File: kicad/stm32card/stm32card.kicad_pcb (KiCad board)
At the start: 2 copper layers, 48 parts, among them SW1 TSD003A04126A02, SW2 TSD003A04126A02, SW3 TSD003A04126A02, SW4 TSD003A04126A02, SW5 TSD003A04126A02, SW6 TSD003A04126A02, SW8 TSD003A04126A02, U2 MT9216, U3 N096-1608TBBIG11-H13, U4 STM32F103C8T6

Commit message: rev1a
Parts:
- removed BAT1, BAT2, BAT3, BAT4: 2997, indigos_kicad_lib:2997_KEY
- removed C20: 10uF, Capacitor_SMD:C_0603_1608Metric
- removed C21: 100nF, Capacitor_SMD:C_0603_1608Metric
- removed the C3 at (91.2, 105.5)
- removed the C6 at (91.2, 113.1)
- removed the R3 at (99.2, 110.5)
- removed SW8: TSD003A04126A02, easyeda2kicad:SW-SMD_4P-L6.0-W6.0-P4.50-LS8.6
- added G***: LOGO, LOGO, F.Cu at (139.8, 122.7)
- added G***: LOGO, LOGO, F.Cu at (139.8, 112.1)
- added G***: LOGO, LOGO, B.Cu at (154.5, 103.7)
- added J1: USB_C_Receptacle_PowerOnly_6P, indigos_kicad_lib:SAMESKY_UJC-H-G-SMT-2-P6-TR, F.Cu at (142.1, 84.3)
- added R1: 5.1k, Resistor_SMD:R_0603_1608Metric, F.Cu at (141.3, 90.8)
- added R2: 5.1k, Resistor_SMD:R_0603_1608Metric, F.Cu at (142.8, 90.8)
- added SWCLK1: SWCLK, TestPoint:TestPoint_Pad_D2.0mm, F.Cu at (165.3, 129.6)
- added SWDIO1: SWDIO, TestPoint:TestPoint_Pad_D2.0mm, F.Cu at (164.8, 124.3)
- added TP1: 675_positive, TestPoint:TestPoint_Pad_4.0x4.0mm, F.Cu at (151.3, 90.0)
- added TP_mosi1: TestPoint, TestPoint:TestPoint_Pad_D2.0mm, F.Cu at (174.4, 114.2)
- added TP_sck1: TestPoint, TestPoint:TestPoint_Pad_D2.0mm, F.Cu at (178.4, 108.9)
- added TestPoint_gnd1: TestPoint_gnd, TestPoint:TestPoint_Pad_D2.0mm, F.Cu at (155.7, 99.1)
- added U2: LM66100DCK, Package_TO_SOT_SMD:SOT-363_SC-70-6, F.Cu at (145.0, 96.6)
- added U3: LM66100DCK, Package_TO_SOT_SMD:SOT-363_SC-70-6, F.Cu at (148.4, 96.6)
- added U6: ~, Library:battery_holder, F.Cu at (167.8, 90.0)
- added tst_nrst1: tst_nrst, TestPoint:TestPoint_Pad_D2.0mm, F.Cu at (180.0, 127.3)
- added unreg_vcc1: unreg_vcc, TestPoint:TestPoint_Pad_D2.0mm, F.Cu at (159.0, 99.1)
- C1: value 4.7uF -> 10uF
- C8: value 10uF -> 2.2uF
- L1: footprint Inductor_SMD:L_0603_1608Metric -> indigos_kicad_lib:IND-SMD_L5.8-W5.2
- R3: renamed from R1; footprint Resistor_SMD:R_0603_1608Metric -> Resistor_SMD:R_0805_2012Metric
- R4: renamed from R2; value 100k 1% -> 100k .01%; footprint Resistor_SMD:R_0603_1608Metric -> Resistor_SMD:R_0805_2012Metric
- moved b_left1 132.0 mm to (215.0, 115.4)
- moved b_down1 131.3 mm to (207.0, 123.8), turned to 180 degrees
- moved b_up1 128.3 mm to (207.0, 106.9)
- moved b_right1 119.0 mm to (199.0, 115.4)
- moved C14 92.9 mm to (187.4, 122.4)
- moved C16 92.4 mm to (187.3, 120.5)
- moved C15 92.0 mm to (187.3, 118.0)
- moved C8 87.8 mm to (179.0, 121.7), turned to 180 degrees
- moved C5 87.8 mm to (179.0, 123.1)
- moved C13 87.7 mm to (182.5, 116.4)
- moved R6 85.4 mm to (184.4, 122.4)
- moved R9 85.1 mm to (184.3, 120.5)
- moved C12 84.2 mm to (176.7, 126.8)
- moved C6 83.7 mm to (174.9, 128.5)
- moved C11 83.3 mm to (179.0, 124.6)
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- renumbered C19 to C11, C17 to C15, C15 to C16, C16 to C17, C5 to C2, C4 to C3, C7 to C4, C9 to C5, C11 to C6, C2 to C9, R11 to R10, R12 to R11, R7 to R12, R9 to R13, R4 to R5, R5 to R6, R8 to R7, R10 to R8, R6 to R9, U2 to U1, U3 to U5, SW4 to b_a1, SW6 to b_b1, SW2 to b_down1, SW5 to b_left1, SW3 to b_right1, SW1 to b_up1
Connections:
- net Net-(U2-EN) renamed unregulated_vcc
- net reset_button renamed Net-(U4-NRST)
- C13 pad 2: Net-(C13-Pad2) -> in_button_up
- C14 pad 2: Net-(C14-Pad2) -> in_button_down
- C15 pad 2: Net-(C17-Pad2) -> in_button_left
- C16 pad 2: Net-(C15-Pad2) -> in_button_right
- C17 pad 2: Net-(C16-Pad2) -> in_button_a
- C18 pad 2: Net-(C18-Pad2) -> in_button_b
- C8 pad 1: +3V0 -> GND
- C8 pad 2: GND -> +3V0
- U4 pad 10: unconnected-(U4-PA0-WKUP-Pad10) -> in_button_down
- U4 pad 11: unconnected-(U4-PA1-Pad11) -> in_button_right
- U4 pad 12: unconnected-(U4-PA2-Pad12) -> in_button_left
- U4 pad 13: unconnected-(U4-PA3-Pad13) -> in_button_up
- U4 pad 18: button_up -> lcd_dataselect
- U4 pad 19: button_down -> lcd_reset
- U4 pad 20: button_left -> lcd_cs
- U4 pad 25: unconnected-(U4-PB12-Pad25) -> power_info
- U4 pad 26: unconnected-(U4-PB13-Pad26) -> in_button_a
- U4 pad 27: unconnected-(U4-PB14-Pad27) -> in_button_b
- U4 pad 34: unconnected-(U4-PA13-Pad34) -> Net-(U4-PA13)
- U4 pad 37: unconnected-(U4-PA14-Pad37) -> Net-(U4-PA14)
- U4 pad 39: button_right -> unconnected-(U4-PB3-Pad39)
- U4 pad 40: button_a -> unconnected-(U4-PB4-Pad40)
- U4 pad 41: button_b -> unconnected-(U4-PB5-Pad41)
- U4 pad 42: Net-(U3-CS) -> unconnected-(U4-PB6-Pad42)
- U4 pad 43: Net-(U3-RESET) -> unconnected-(U4-PB7-Pad43)
- U4 pad 45: Net-(U3-RS) -> unconnected-(U4-PB8-Pad45)
- U5 pad 5: Net-(U3-RS) -> lcd_dataselect
- U5 pad 6: Net-(U3-RESET) -> lcd_reset
- U5 pad 7: Net-(U3-CS) -> lcd_cs
- b_a1 pad 3: button_a -> in_button_a
- b_a1 pad 4: Net-(C16-Pad2) -> in_button_a
- b_b1 pad 3: button_b -> in_button_b
- b_b1 pad 4: Net-(C18-Pad2) -> in_button_b
- b_down1 pad 3: button_down -> in_button_down
- b_down1 pad 4: Net-(C14-Pad2) -> in_button_down
- b_left1 pad 3: button_left -> in_button_left
- b_left1 pad 4: Net-(C17-Pad2) -> in_button_left
- b_right1 pad 3: button_right -> in_button_right
- b_right1 pad 4: Net-(C15-Pad2) -> in_button_right
- b_up1 pad 3: button_up -> in_button_up
- b_up1 pad 4: Net-(C13-Pad2) -> in_button_up
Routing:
- net +3V0: track 0.00 -> 257.7 mm
- net GND: track 0.00 -> 190.9 mm, vias 0 -> 34
- net in_button_left: track 0.00 -> 44.4 mm
- net in_button_up: track 0.00 -> 40.0 mm
- net power_info: track 0.00 -> 39.5 mm
- net in_button_down: track 0.00 -> 35.8 mm
- net in_button_a: track 0.00 -> 30.9 mm
- net in_button_right: track 0.00 -> 28.8 mm
- net in_button_b: track 0.00 -> 27.8 mm
- net unregulated_vcc: track 0.00 -> 23.0 mm
- net Net-(U2-~{CE}): track 0.00 -> 18.7 mm
- net spi1_sck: track 0.00 -> 15.6 mm
- net spi1_mosi: track 0.00 -> 14.9 mm
- net lcd_cs: track 0.00 -> 13.6 mm
- net lcd_reset: track 0.00 -> 12.6 mm
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- added copper zone on B.Cu, net GND
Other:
- board outline added: 88.9 x 50.8 mm
- board text added: "(913) 228-6776"
- board text added: "Brett Weiland"
- board text added: "Electrical and Computer Engineer"
- board text added: "bpcspace.com"
- board text added: "brettsweiland@gmail.com"
- board text added: "mandrelcard.alpha.01"
- board text removed: "CHECK PAGAGES!!!!! 10/40k resistor, inductor are wrong!!!"

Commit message: applying 4 more jobs
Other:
- board text added: "BEFORE RE-ORDERING: - fix routing to MCU; footprint was changed - fix vtext - SPI NSI - LEDs? - change your god damn test pins - remove if no more needed - remove button outlines - SPI speed stuck at 2mHZ - differential routing? - LCD backlight MOSFTER - test to see if sleep mode is accurate to datasheet - screen responds in sleep mode, which is sus - add mosfet to LED VDD if above is too sus"

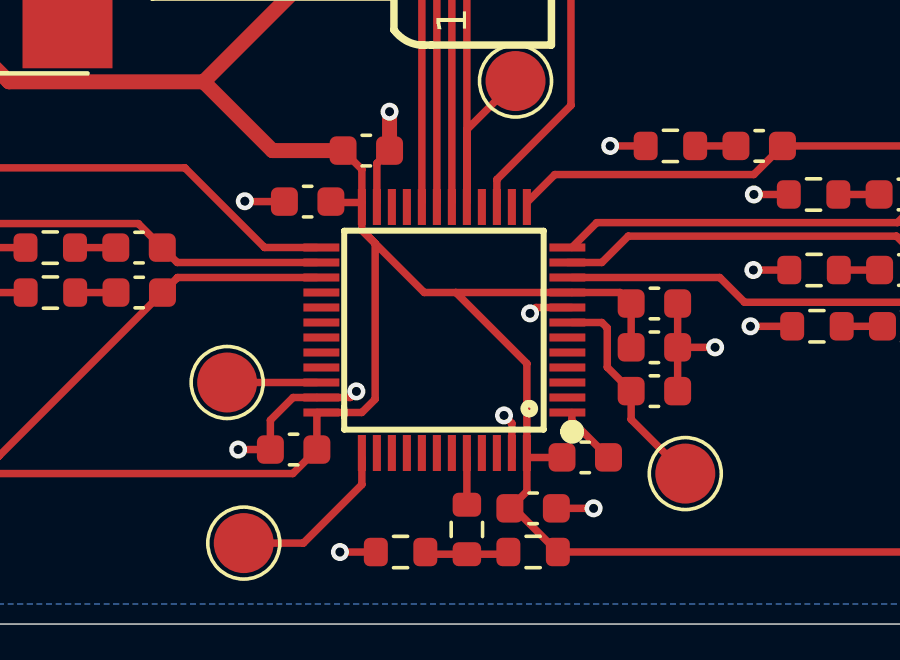
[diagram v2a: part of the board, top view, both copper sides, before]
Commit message: optimized spi
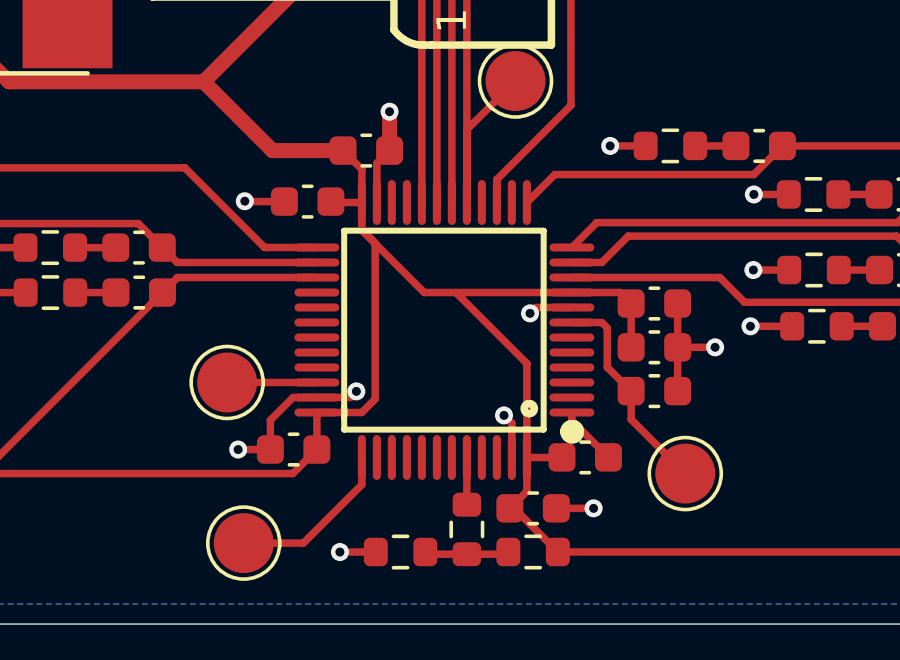
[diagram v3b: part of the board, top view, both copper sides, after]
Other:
- board text removed: "BEFORE RE-ORDERING: - fix routing to MCU; footprint was changed - fix vtext - SPI NSI - LEDs? - change your god damn test pins - remove if no more needed - remove button outlines - SPI speed stuck at 2mHZ - differential routing? - LCD backlight MOSFTER - test to see if sleep mode is accurate to datasheet - screen responds in sleep mode, which is sus - add mosfet to LED VDD if above is too sus"

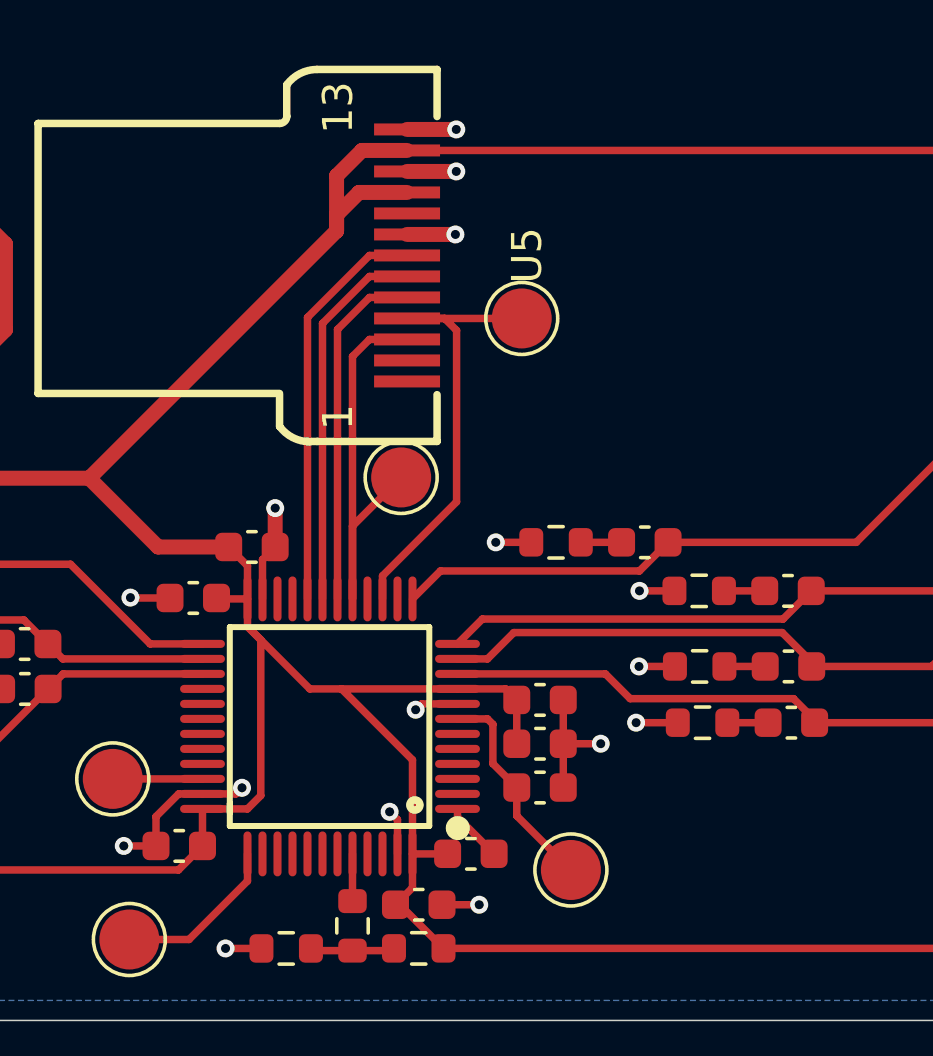
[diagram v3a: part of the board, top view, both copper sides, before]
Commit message: optimized spi
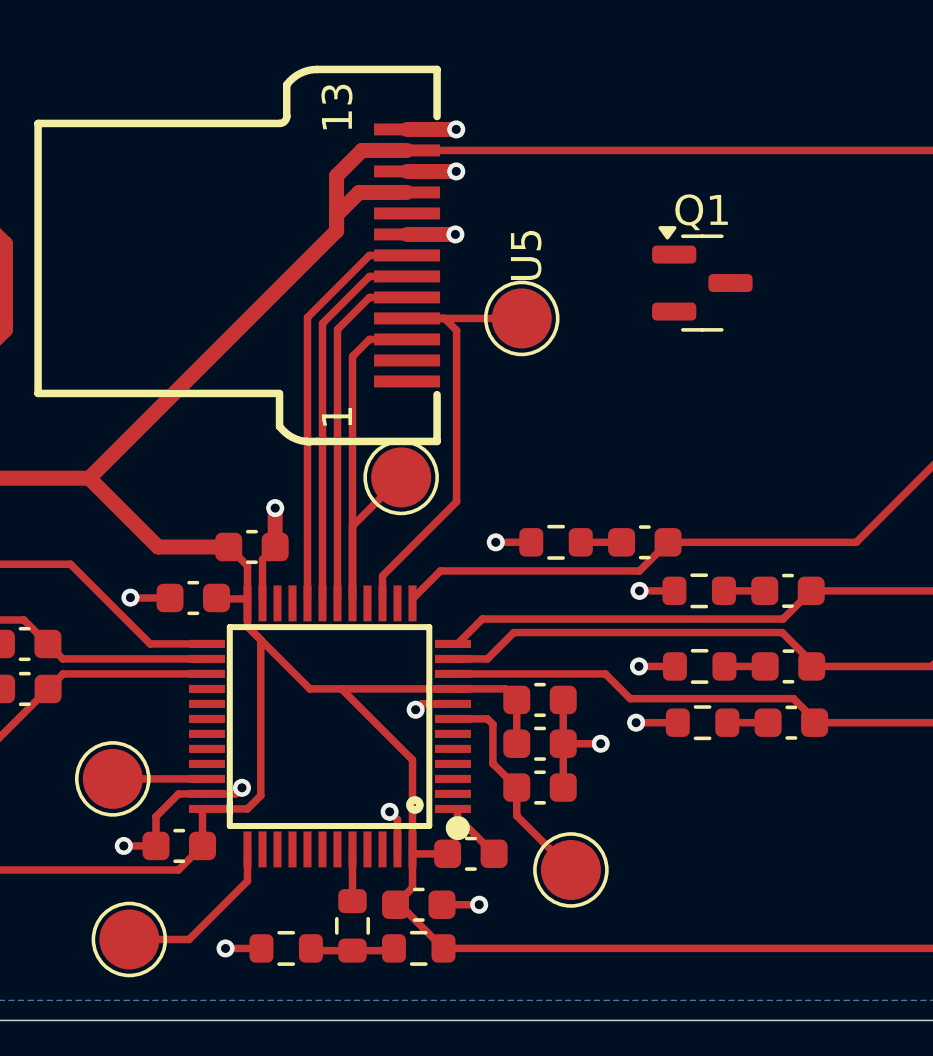
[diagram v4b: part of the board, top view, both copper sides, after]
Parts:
- added Q1: AO3400A, Package_TO_SOT_SMD:SOT-23, F.Cu at (184.4, 107.8)
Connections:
- U4 pad 21: unconnected-(U4-PB10-Pad21) -> backlight_fet
- U5 pad 12: +3V0 -> Net-(Q1-S)
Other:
- board text added: "BEFORE RE-ORDERING: - fix routing to MCU; footprint was changed - fix vtext - SPI NSI - LEDs? - change your god damn test pins - remove if no more needed - remove button outlines - SPI speed stuck at 2mHZ - differential routing? - LCD backlight MOSFTER - test to see if sleep mode is accurate to datasheet - screen responds in sleep mode, which is sus - add mosfet to LED VDD if above is too sus"

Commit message: about to add border tracing, thick in the weeds
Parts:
- removed the G*** at (139.8, 112.1)
- moved Q1 26.3 mm to (159.3, 115.5), turned to 180 degrees
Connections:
- U4 pad 21: backlight_fet -> unconnected-(U4-PB10-Pad21)
- U4 pad 28: unconnected-(U4-PB15-Pad28) -> backlight_fet
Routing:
- net Net-(Q1-S): track 0.00 -> 18.4 mm
- net backlight_fet: track 0.00 -> 12.9 mm
- net +3V0: track 257.7 -> 253.7 mm

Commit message: need to organize, redid PCB
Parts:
- removed R3: 400k 1%, Resistor_SMD:R_0805_2012Metric
- removed unreg_vcc1: unreg_vcc, TestPoint:TestPoint_Pad_D2.0mm
- added BT1: NiMH AAA cell, Battery:BatteryHolder_Keystone_2466_1xAAA, F.Cu at (171.7, 90.8)
- added C19: 1nF, Capacitor_SMD:C_0603_1608Metric, F.Cu at (154.8, 111.9)
- added C20: 1uF, Capacitor_SMD:C_0603_1608Metric, F.Cu at (155.5, 117.2)
- added C21: 1uF, Capacitor_SMD:C_0603_1608Metric, F.Cu at (153.6, 119.1)
- added C22: 10uF, Capacitor_SMD:C_0603_1608Metric, F.Cu at (159.8, 109.5)
- added C24: 1uF, Capacitor_SMD:C_0603_1608Metric, F.Cu at (155.2, 124.4)
- added C25: 10uF, Capacitor_SMD:C_0603_1608Metric, F.Cu at (159.0, 107.2)
- added C7: 270nF, Capacitor_SMD:C_0805_2012Metric, F.Cu at (151.2, 97.2)
- added D1: D_Schottky, Diode_SMD:D_SMA, F.Cu at (162.7, 86.8)
- added D2: purple, LED_SMD:LED_0805_2012Metric, F.Cu at (163.3, 92.0)
- added D3: amber, LED_SMD:LED_0603_1608Metric, F.Cu at (163.1, 93.9)
- added G***: LOGO, LOGO, F.Cu at (139.1, 113.5)
- added L2: 4.7uH, indigos_imports:IND-SMD_L5.8-W5.2, F.Cu at (156.6, 103.0)
- added Q2: XR2N13, Package_TO_SOT_SMD:SOT-23, F.Cu at (158.9, 123.2)
- added R14: 50, Resistor_SMD:R_0603_1608Metric, F.Cu at (163.0, 97.1)
- added R15: 50, Resistor_SMD:R_0603_1608Metric, F.Cu at (163.0, 95.5)
- added R16: 500k 1%, Resistor_SMD:R_0603_1608Metric, F.Cu at (158.2, 109.5)
- added R17: 100k 1%, Resistor_SMD:R_0603_1608Metric, F.Cu at (159.0, 111.8)
- added R18: 400k 1%, Resistor_SMD:R_0603_1608Metric, F.Cu at (153.6, 126.0)
- added R19: 100k 1%, Resistor_SMD:R_0603_1608Metric, F.Cu at (155.3, 127.8)
- added R20: 10k, Resistor_SMD:R_0603_1608Metric, F.Cu at (154.8, 110.3)
- added R21: 0, Resistor_SMD:R_0603_1608Metric, F.Cu at (166.6, 89.6)
- added R22: 10k, Resistor_SMD:R_0603_1608Metric, F.Cu at (157.4, 126.0)
- added R23: 10k, Resistor_SMD:R_0603_1608Metric, F.Cu at (160.6, 126.0)
- added R24: 0, Resistor_SMD:R_0603_1608Metric, F.Cu at (161.2, 116.5)
- added TP2: tp_usb, TestPoint:TestPoint_Pad_D2.0mm, F.Cu at (134.9, 88.3)
- added TP3: tp_3v, TestPoint:TestPoint_Pad_D2.0mm, F.Cu at (162.2, 129.6)
- added U7: BU4210G-TR, indigos_imports:SSOP-5_L2.9-W1.6-P0.95-LS2.8-TL, F.Cu at (154.8, 114.5)
- added U9: CJ6300BM, indigos_imports:SOT-23-5_L2.9-W1.6-P0.95-LS2.8-BR, F.Cu at (153.5, 121.9)
- C1: value 10uF -> 22uF
- C10: value 10uF -> 15nF
- C9: value 22pF -> 22uF
- L1: value 4.7uH -> 15uH; footprint indigos_kicad_lib:IND-SMD_L5.8-W5.2 -> indigos_imports:IND-SMD_L7.2-W6.6_GPSR07X0
- Q1: value AO3400A -> XR2N13
- R4: value 100k .01% -> 0; footprint Resistor_SMD:R_0805_2012Metric -> Resistor_SMD:R_0603_1608Metric
- TP1: value 675_positive -> tp_battery; footprint TestPoint:TestPoint_Pad_4.0x4.0mm -> TestPoint:TestPoint_Pad_D2.0mm
- TestPoint_gnd1: value TestPoint_gnd -> tp_gnd
- U1: value MT9216 -> CN3600; footprint easyeda2kicad:SOT-23-5_L3.0-W1.7-P0.95-LS2.8-BL -> indigos_imports:ESOP-8_L4.9-W3.9-P1.27-LS6.0-BL-EP
- U6: value ~ -> TLV61220DBVR-TP; footprint Library:battery_holder -> indigos_imports:SOT-23-6_L2.9-W1.6-P0.95-LS2.8-BL
- moved U3 25.3 mm to (159.0, 119.6), turned to 0 degrees
- moved L1 24.4 mm to (156.0, 86.7)
- moved U2 24.2 mm to (158.9, 116.3)
- moved U6 22.1 mm to (154.8, 107.9), turned to -90 degrees
- moved TP1 16.7 mm to (166.6, 96.7)
- moved TestPoint_gnd1 16.5 mm to (166.3, 86.5)
- moved C9 12.6 mm to (152.0, 94.0)
- moved C1 10.9 mm to (158.7, 91.8), turned to 180 degrees
- moved R4 10.5 mm to (155.4, 91.8), turned to 180 degrees
- moved U1 8.12 mm to (156.6, 95.5), turned to 90 degrees
- moved C10 6.65 mm to (159.0, 113.5)
- moved Q1 4.91 mm to (164.0, 117.0)
- moved R12 3.54 mm to (162.3, 120.5)
- moved C17 3.54 mm to (165.3, 120.5)
- moved C18 3.40 mm to (165.1, 122.2)
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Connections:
- C1 pad 1: unregulated_vcc -> Net-(D1-K)
- C10 pad 1: +3V0 -> Net-(U7-CT)
- C9 pad 1: +3V0 -> usb vbus
- C9 pad 2: Net-(U1-FB) -> GND
- J1 pad A9: Net-(U2-~{CE}) -> usb vbus
- J1 pad B9: Net-(U2-~{CE}) -> usb vbus
- L1 pad 2: +3V0 -> Net-(D1-A)
- R4 pad 1: Net-(U1-FB) -> Net-(U1-ISEL)
- TP1 pad 1: Net-(U2-VIN) -> bat output
- U1 pad 1: unregulated_vcc -> Net-(U1-~{CHRG})
- U1 pad 2: GND -> Net-(U1-ISEL)
- U1 pad 3: unregulated_vcc -> Net-(D1-K)
- U1 pad 4: Net-(U1-FB) -> GND
- U2 pad 3: Net-(U2-~{CE}) -> usb vbus
- U2 pad 5: power_info -> unconnected-(U2-ST-Pad5)
- U2 pad 6: unregulated_vcc -> Net-(U2-VOUT)
- U3 pad 1: Net-(U2-~{CE}) -> Net-(U3-VIN)
- U3 pad 3: Net-(U2-VIN) -> Net-(Q2-D)
- U3 pad 5: GND -> power_info
- U3 pad 6: unregulated_vcc -> Net-(U2-VOUT)
- U6 pad 1: GND -> Net-(U6-SW)
- U6 pad 3: GND -> Net-(U6-EN)
- U6 pad 4: GND -> Net-(U6-FB)
- b_a1 pad 4: in_button_a -> unconnected-(b_a1-Pad4)
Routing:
- net GND: track 190.7 -> 75.7 mm, vias 34 -> 41
- net usb vbus: track 0.00 -> 109.1 mm
- net bat output: track 0.00 -> 38.7 mm
- net power_info: track 39.5 -> 8.07 mm
- net unregulated_vcc: track 23.0 -> 0.00 mm
- net +3V0: track 253.7 -> 234.7 mm
- net Net-(U2-~{CE}): track 18.7 -> 0.00 mm
- net Net-(D1-K): track 0.00 -> 13.6 mm
- net Net-(U1-~{DONE}): track 0.00 -> 9.71 mm
- net in_button_a: track 30.9 -> 40.0 mm
- net Net-(U3-VIN): track 0.00 -> 9.04 mm
- net Net-(Q2-D): track 0.00 -> 7.54 mm
- net Net-(U1-FB): track 6.20 -> 0.00 mm
- net Net-(U1-ISEL): track 0.00 -> 6.15 mm
- net Net-(U9-FB): track 0.00 -> 5.81 mm
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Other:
- board text added: "Make sure CN36000 package and connections are right on PCB - wtf is EP?"
- board text added: "PERSONAL TODO"
- board text added: "chrg"
- board text added: "full"
- board text removed: "mandrelcard.alpha.01"
